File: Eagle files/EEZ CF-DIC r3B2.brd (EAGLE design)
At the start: 155 x 85 mm, 240 parts, among them IC1 MC79L05, IC2 LP2951, IC3 VIPer35L, IC4 SI8233BB-D-IS1, IC5 LM5041B, IC6 IR11688STRPBF, IC7 TL072, IC8 TL103W, IC9 TL431, P1 T910W-50K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

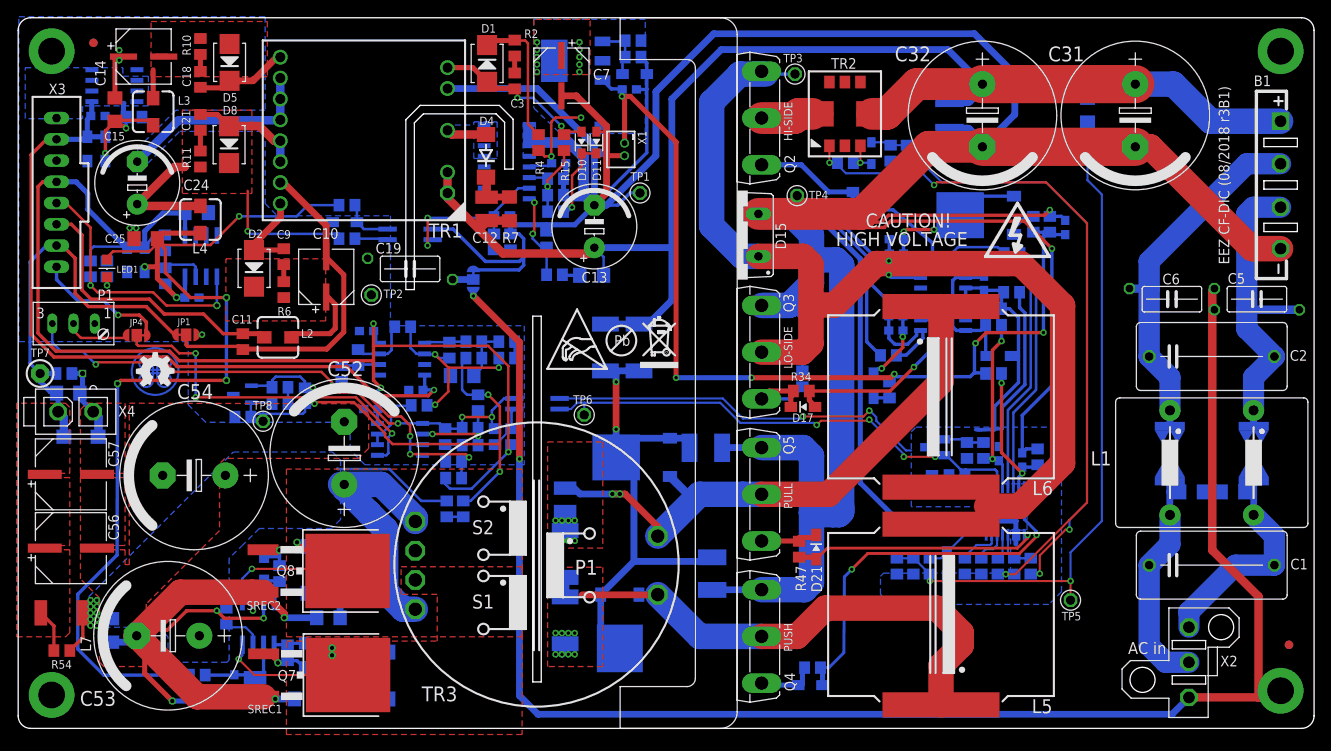
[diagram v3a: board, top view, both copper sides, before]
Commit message: BOM update, optional RC added at the output terminals
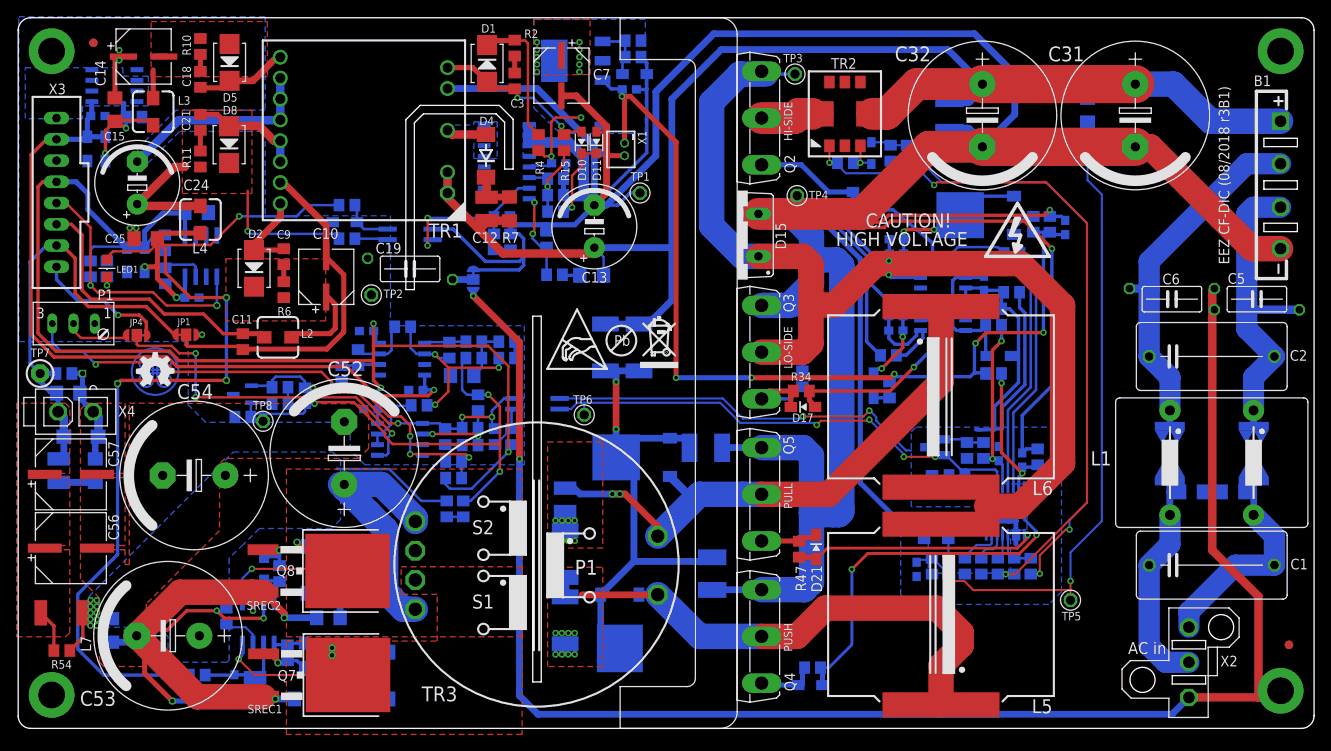
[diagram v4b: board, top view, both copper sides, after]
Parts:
- added C74: N.C., rcl:C0805
- added R80: N.C., rcl:R0805
- C42: device rcl:C0805 -> rcl:C0603
- C60: value 4n7/200V -> N.C.
- C61, C65: value 100n -> 4n7/200V; device rcl:C0603 -> rcl:C1206
- C62: value 10u -> 100n; device rcl:C1210 -> rcl:C0603
- C63: value 100n -> 10u; device rcl:C0603 -> rcl:C1210
- C64: value 4n7/200V -> 100n; device rcl:C1206 -> rcl:C0603
- C67: value 100p -> 100n; device rcl:C0805 -> rcl:C0603
- C69: value 33n -> 100p
- C70: value 4u7 -> 33n; device EEZ_Lib1:EC1206 -> rcl:C0805
- C71: value 1u -> 4u7; device rcl:C0805 -> EEZ_Lib1:EC1206
- C72: value N.C. -> 1u
- R55: value 22R/3W -> N.C.; device rcl:R2512 -> rcl:R1210
- R57: value 3R3 -> 22R/3W; device rcl:R0805 -> rcl:R2512
- R58: value 10R -> 3R3
- R59: value 47K -> 10R
- R60: value 3R3 -> 47K
- R61: value 22R/3W -> 3R3; device rcl:R2512 -> rcl:R0805
- R63: value 10K -> 22R/3W; device rcl:R0805 -> rcl:R2512
- R64: value 316K -> 10K
- R65: value 10K -> 316K
- R66: value 750R -> 10K
- R67: value 0R -> 750R
- R68: value 750R -> 0R
- R69: value 470R -> 750R
- R70: value 12K -> 470R
- R71: value 3K3 -> 12K
- R72: value 750R -> 3K3
- R73: value 30K -> 750R
- R74: value 10K -> 30K
- R75: value 16K -> 10K
- R76: value 220R -> 16K
- R77: value N.C. -> 220R
- moved C63 44.9 mm to (33.3, 6.67), turned to 270 degrees
- moved R55 42.5 mm to (9.84, 32.8), turned to 90 degrees
- moved C60 37.2 mm to (14.2, 32.8), turned to 270 degrees
- moved C64 34.6 mm to (46.7, 49.5)
- moved C65 29.2 mm to (42.1, 15.2)
- moved R78 26.0 mm to (62.0, 36.9), turned to 90 degrees
- moved R63 25.4 mm to (44.3, 21.0)
- moved R64 21.0 mm to (45.7, 46.4), turned to 270 degrees
- moved R65 20.5 mm to (56.3, 28.3), turned to 90 degrees
- moved R66 20.1 mm to (43.7, 44.5), turned to 270 degrees
- moved C72 19.4 mm to (57.1, 33.9), turned to 0 degrees
- moved R69 18.5 mm to (51.0, 50.0), turned to 0 degrees
- moved R68 13.0 mm to (63.4, 46.3)
- moved C67 11.7 mm to (47.2, 40.2), turned to 0 degrees
- moved R77 11.6 mm to (59.5, 48.3), turned to 0 degrees
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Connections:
- new net N$8: C60.2, R55.1
- net +6V: now also R59.1; no longer R58.1
- net FB: now also C73.2, R71.1, R76.2, R80.2; no longer C72.2, R70.1, R74.2, R78.2
- net GND: now also C60.1, C67.2, C71.-, C72.2, R60.2, R80.1; no longer C60.2, C70.-, C71.2, R59.2, R79.1
- net N$1: now also C68.2, R68.2, R69.1, R73.1; no longer C67.2, R67.2, R68.1, R72.1
- net N$10: now also C69.2, R75.1; no longer C68.2, R73.1
- net N$12: now also R65.1, R71.2; no longer R64.1, R70.2
- net N$132: now also R64.2, R66.1; no longer R63.2, R65.1
- net N$134: now also C68.1, R77.2; no longer C67.1, R76.2
- net N$17: now also C74.2, R79.1; no longer C73.2, R78.1
- net N$18: now also R60.1; no longer R59.1
- net N$53: now also R64.1, R69.2; no longer R63.1, R68.2
- net N$6: now also C63.1, R59.2; no longer C61.1, R58.2
- net N$64: now also R67.2, R68.1; no longer R66.2, R67.1
- net N$66: now also C61.1, R57.2; no longer C60.1, R55.2
- net N$67: now also C65.1, R63.2; no longer C64.1, R61.2
- net N$7: now also C72.1, R66.2, R72.1; no longer C71.1, R65.2, R71.1
- net N$74: now also R58.2; no longer R57.2
- net N$75: now also R61.2; no longer R60.2
- net N$76: now also C70.1, C74.1, R78.2; no longer C68.1, C72.1, R77.2
- net N$9: now also C70.2, R74.2; no longer C69.2, R73.2
- net NFB_OFFSET: now also C71.+, R67.1, R77.1; no longer C70.+, R66.1, R75.1
- net OK_A: now also R70.1, R78.1; no longer R69.1, R77.1
- net POUT+: now also R65.2; no longer R64.2
- net PREG_OUT+: now also R55.2
- net S1_DOT_OUT: now also R57.1; no longer R55.1
- net S2_OUT: now also R63.1; no longer R61.1
- net SR_OUT1: now also R58.1; no longer R57.1
- net SR_OUT2: now also R61.1; no longer R60.1
- net U_MON1: now also R73.2; no longer R72.2
- net V+: now also C64.1, C67.1, R70.2, R72.2; no longer C63.1, C66.1, R69.2, R71.2
- net V-: now also C66.1; no longer C65.1
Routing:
- net N$8: track 0.00 -> 4.38 mm
- net PREG_OUT+: track 55.2 -> 58.2 mm
- net GND: track 137.9 -> 140.7 mm
- net ULVO: track 77.4 -> 76.0 mm
- net N$25: track 7.91 -> 7.04 mm
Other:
- board text added: "C74"
- board text added: "R80"

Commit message: modified thermals for output bulk capacitors
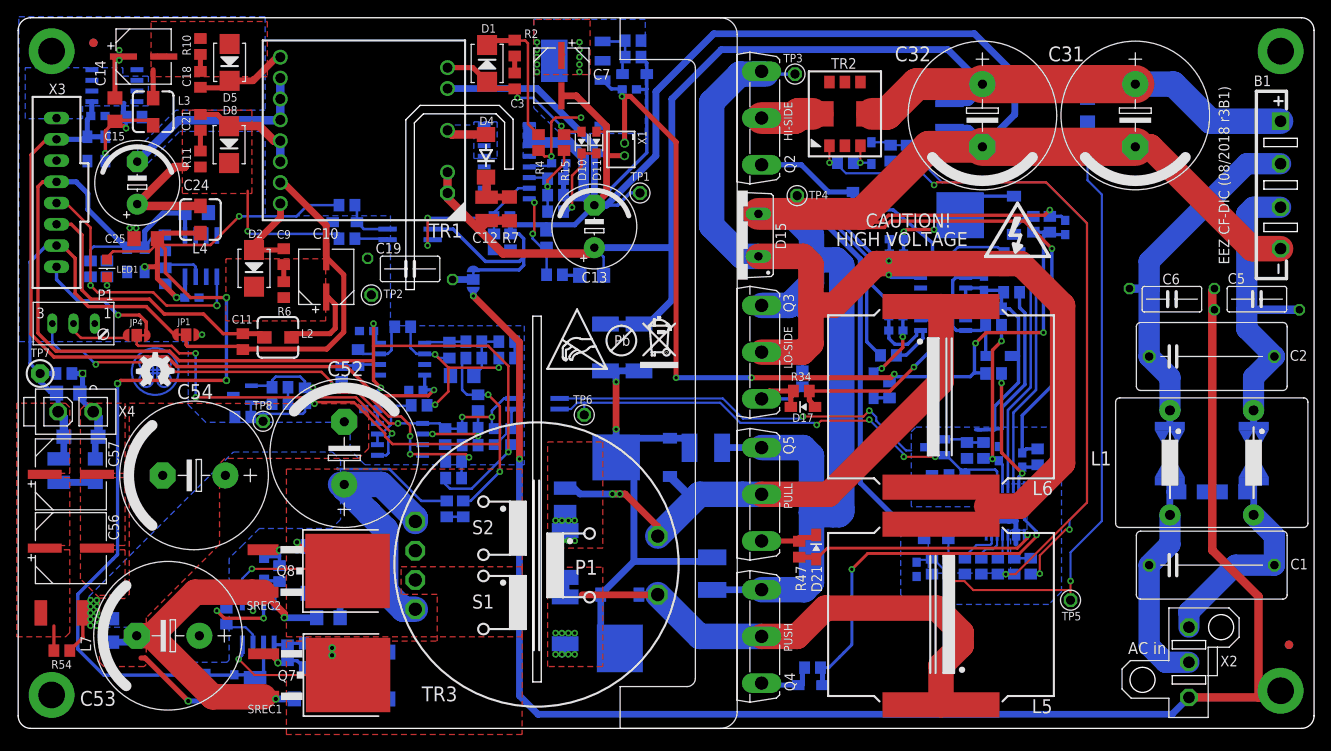
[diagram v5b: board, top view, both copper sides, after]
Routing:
- net GND: track 140.7 -> 123.9 mm
- net PREG_OUT+: track 58.2 -> 55.9 mm
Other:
- board text added: "Licensed under the TAPR Open Hardware License (www.tapr.org/OHL)"
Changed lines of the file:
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@@
 <layer number="17" name="Pads" color="14" fill="1" visible="yes" active="yes"/>
 <layer number="18" name="Vias" color="6" fill="1" visible="yes" active="yes"/>
-<layer number="19" name="Unrouted" color="6" fill="1" visible="no" active="yes"/>
+<layer number="19" name="Unrouted" color="6" fill="1" visible="yes" active="yes"/>
 <layer number="20" name="Dimension" color="4" fill="1" visible="yes" active="yes"/>
 <layer number="21" name="tPlace" color="7" fill="1" visible="yes" active="yes"/>
 <layer number="22" name="bPlace" color="6" fill="1" visible="yes" active="yes"/>
-<layer number="23" name="tOrigins" color="15" fill="1" visible="no" active="yes"/>
-<layer number="24" name="bOrigins" color="15" fill="1" visible="no" active="yes"/>
+<layer number="23" name="tOrigins" color="15" fill="1" visible="yes" active="yes"/>
+<layer number="24" name="bOrigins" color="15" fill="1" visible="yes" active="yes"/>
 <layer number="25" name="tNames" color="7" fill="1" visible="yes" active="yes"/>
 <layer number="26" name="bNames" color="5" fill="1" visible="yes" active="yes"/>
@@
 <layer number="45" name="Holes" color="7" fill="1" visible="no" active="yes"/>
 <layer number="46" name="Milling" color="3" fill="1" visible="no" active="yes"/>
-<layer number="47" name="Measures" color="7" fill="1" visible="no" active="yes"/>
+<layer number="47" name="Measures" color="7" fill="1" visible="yes" active="yes"/>
 <layer number="48" name="Document" color="7" fill="1" visible="no" active="yes"/>
 <layer number="49" name="Reference" color="7" fill="1" visible="no" active="yes"/>
@@
 <text x="112.478996875" y="24.177496875" size="1.016" layer="126" ratio="10" rot="MR0">ZD5</text>
 <text x="15.7115" y="37.512496875" size="1.27" layer="126" ratio="10" rot="MR180">ZD6</text>
+<text x="5.207" y="-1.016" size="1.27" layer="47" ratio="10">Licensed under the TAPR Open Hardware License (www.tapr.org/OHL)</text>
 </plain>
 <attributes>
@@
 </polygon>
 <wire x1="9.2735" y1="11.303" x2="9.2735" y2="14.2469" width="0.4064" layer="1"/>
-<wire x1="9.2735" y1="14.2469" x2="7.7089" y2="15.8115" width="0.4064" layer="1"/>
 <contactref element="X3" pad="2"/>
 <wire x1="23.9395" y1="49.0855" x2="23.6855" y2="49.0855" width="0.4064" layer="1"/>
@@
 <wire x1="34.3535" y1="17.205" x2="34.3535" y2="15.1765" width="0.4064" layer="16"/>
 <via x="34.3535" y="15.1765" extent="1-16" drill="0.4" shape="octagon"/>
-<via x="23.4315" y="5.2705" extent="1-16" drill="0.5" shape="octagon"/>
+<via x="25.3365" y="5.2705" extent="1-16" drill="0.5" shape="octagon"/>
 <via x="28.7655" y="16.0655" extent="1-16" drill="0.4" shape="octagon"/>
 <wire x1="28.7655" y1="16.0655" x2="29.5935" y2="16.0655" width="0.254" layer="16"/>
 <wire x1="29.5935" y1="16.0655" x2="29.9085" y2="16.3805" width="0.254" layer="16"/>
-<wire x1="23.4315" y1="5.2705" x2="23.6885" y2="5.2675" width="0.6096" layer="16"/>
-<wire x1="23.6885" y1="5.2675" x2="30.861" y2="5.2675" width="0.6096" layer="16"/>
+<wire x1="25.3365" y1="5.2705" x2="27.816" y2="5.2675" width="0.6096" layer="16"/>
+<wire x1="27.816" y1="5.2675" x2="30.861" y2="5.2675" width="0.6096" layer="16"/>
 <wire x1="30.861" y1="5.2675" x2="33.3375" y2="5.2675" width="0.6096" layer="16"/>
 <wire x1="30.861" y1="6.7065" x2="30.861" y2="5.2675" width="0.6096" layer="16"/>
-<wire x1="23.4315" y1="5.2705" x2="20.1295" y2="8.5725" width="0.6096" layer="1"/>
-<wire x1="20.1295" y1="8.5725" x2="20.1295" y2="12.446" width="0.6096" layer="1"/>
+<wire x1="25.3365" y1="5.2705" x2="20.193" y2="10.414" width="0.6096" layer="1"/>
 <contactref element="C55" pad="2"/>
 <contactref element="C61" pad="2"/>
@@
 <contactref element="C56" pad="2"/>
 <contactref element="X4" pad="2"/>
-<wire x1="34.3535" y1="5.7785" x2="26.4125" y2="5.7785" width="3.048" layer="1"/>
-<wire x1="26.4125" y1="5.7785" x2="19.1735" y2="13.081" width="3.048" layer="1"/>
+<wire x1="34.3535" y1="5.7785" x2="28.2575" y2="5.7785" width="3.048" layer="1"/>
 <wire x1="34.294" y1="18.288" x2="32.9565" y2="18.288" width="3.048" layer="1"/>
-<wire x1="32.9565" y1="18.288" x2="24.3805" y2="18.288" width="3.048" layer="1"/>
-<wire x1="24.3805" y1="18.288" x2="19.1135" y2="13.0175" width="3.048" layer="1"/>
-<wire x1="19.1135" y1="13.0175" x2="19.8755" y2="13.081" width="3.048" layer="1" curve="90"/>
-<wire x1="19.8755" y1="13.081" x2="19.1735" y2="13.081" width="3.048" layer="1"/>
+<wire x1="32.9565" y1="18.288" x2="26.162" y2="18.288" width="3.048" layer="1"/>
 <wire x1="40.7005" y1="15.24" x2="36.83" y2="15.24" width="0.8128" layer="16"/>
 <via x="36.83" y="15.24" extent="1-16" drill="0.5" shape="octagon"/>
-<wire x1="38.0335" y1="5.5245" x2="35.7505" y2="5.5245" width="0.8128" layer="16"/>
-<via x="35.7505" y="5.5245" extent="1-16" drill="0.5" shape="octagon"/>
+<wire x1="38.0335" y1="5.5245" x2="35.814" y2="5.5245" width="0.8128" layer="16"/>
+<via x="35.814" y="5.5245" extent="1-16" drill="0.5" shape="octagon"/>
 <wire x1="33.0835" y1="17.205" x2="33.0835" y2="16.0655" width="0.4064" layer="16"/>
 <via x="33.0835" y="16.0655" extent="1-16" drill="0.4" shape="octagon"/>
-<polygon width="0.254" layer="1" isolate="0.4064" thermals="no">
-<vertex x="13.208" y="40.894"/>
-<vertex x="17.78" y="40.894"/>
-<vertex x="17.78" y="32.512"/>
-<vertex x="16.002" y="32.512"/>
-<vertex x="16.002" y="32.004"/>
-<vertex x="17.78" y="32.004"/>
-<vertex x="17.78" y="23.876"/>
-<vertex x="16.002" y="23.876"/>
-<vertex x="16.002" y="23.368"/>
-<vertex x="17.78" y="23.368"/>
-<vertex x="17.78" y="21.59"/>
-<vertex x="18.288" y="21.59"/>
+<polygon width="0.254" layer="1" isolate="0.4064">
+<vertex x="18.288" y="17.9705"/>
 <vertex x="18.288" y="40.894"/>
 <vertex x="45.6565" y="40.8305"/>
@@
 <vertex x="29.718" y="34.29"/>
 <vertex x="29.083" y="33.655"/>
-<vertex x="29.083" y="25.654"/>
-<vertex x="20.32" y="16.891"/>
+<vertex x="29.083" y="24.003"/>
+<vertex x="20.32" y="15.24"/>
 <vertex x="20.32" y="9.652"/>
 <vertex x="20.066" y="9.398"/>
 <vertex x="15.24" y="9.398"/>
 <vertex x="14.732" y="9.906"/>
-<vertex x="14.732" y="17.5895"/>
-<vertex x="12.446" y="19.8755"/>
-<vertex x="12.446" y="40.132"/>
+<vertex x="14.732" y="17.907"/>
 </polygon>
 <wire x1="24.1935" y1="74.7395" x2="36.3115" y2="74.7395" width="1.016" layer="16"/>
@@
 <wire x1="36.83" y1="15.24" x2="36.83" y2="15.752" width="0.8128" layer="1"/>
 <wire x1="36.83" y1="15.752" x2="34.294" y2="18.288" width="0.8128" layer="1"/>
-<wire x1="28.7655" y1="16.0655" x2="25.146" y2="16.0655" width="0.4064" layer="1"/>
-<wire x1="25.146" y1="16.0655" x2="22.86" y2="13.7795" width="0.4064" layer="1"/>
-<wire x1="22.86" y1="13.7795" x2="19.812" y2="13.7795" width="0.4064" layer="1"/>
-<wire x1="19.812" y1="13.7795" x2="19.177" y2="13.1445" width="0.4064" layer="1"/>
 <wire x1="34.3575" y1="5.842" x2="34.3535" y2="5.5245" width="0.4064" layer="1"/>
-<wire x1="34.3535" y1="5.5245" x2="35.7505" y2="5.5245" width="0.4064" layer="1"/>
+<wire x1="34.3535" y1="5.5245" x2="35.814" y2="5.5245" width="0.4064" layer="1"/>
 <wire x1="16.1925" y1="12.316" x2="18.4085" y2="12.316" width="0.8128" layer="16"/>
 <wire x1="18.4085" y1="12.316" x2="19.1735" y2="13.081" width="0.8128" layer="16"/>
@@
 <wire x1="14.224" y1="34.2295" x2="14.224" y2="36.558" width="0.8128" layer="16"/>
 <wire x1="14.224" y1="36.558" x2="14.5595" y2="36.8935" width="0.8128" layer="16"/>
-<wire x1="34.3535" y1="5.7785" x2="34.3575" y2="5.842" width="0" layer="19" extent="1-1"/>
+<polygon width="0.254" layer="1" isolate="0.4064" thermals="no">
+<vertex x="13.208" y="40.894"/>
+<vertex x="17.78" y="40.894"/>
+<vertex x="17.78" y="32.512"/>
+<vertex x="16.002" y="32.512"/>
+<vertex x="16.002" y="32.004"/>
+<vertex x="17.78" y="32.004"/>
+<vertex x="17.78" y="23.876"/>
+<vertex x="16.002" y="23.876"/>
+<vertex x="16.002" y="23.368"/>
+<vertex x="17.78" y="23.368"/>
+<vertex x="17.78" y="17.526"/>
+<vertex x="14.732" y="17.5895"/>
+<vertex x="12.446" y="19.8755"/>
+<vertex x="12.446" y="40.132"/>
+</polygon>
+<wire x1="20.193" y1="10.414" x2="19.685" y2="10.414" width="0.6096" layer="1"/>
+<wire x1="28.2575" y1="5.7785" x2="20.955" y2="13.081" width="3.048" layer="1"/>
+<wire x1="26.162" y1="18.288" x2="20.955" y2="13.081" width="3.048" layer="1"/>
+<wire x1="20.955" y1="13.081" x2="19.1735" y2="13.081" width="3.048" layer="1"/>
+<wire x1="34.294" y1="18.288" x2="34.3535" y2="17.205" width="0" layer="19" extent="1-16"/>
+<wire x1="34.3575" y1="5.842" x2="34.3535" y2="5.7785" width="0" layer="19" extent="1-1"/>
 </signal>
 <signal name="REF">
@@
 <contactref element="Q4" pad="D"/>
 <contactref element="D19" pad="2"/>
-<polygon width="0.254" layer="1" isolate="0.3048" thermals="no">
+<polygon width="0.254" layer="1" isolate="0.3048">
 <vertex x="74.93" y="9.398"/>
 <vertex x="68.326" y="9.398"/>
@@
 <contactref element="R31" pad="1"/>
 <wire x1="70.4215" y1="27.937" x2="70.4215" y2="25.66" width="1.016" layer="16"/>
-<polygon width="0.254" layer="1" isolate="0.3048" thermals="no">
+<polygon width="0.254" layer="1" isolate="0.3048">
 <vertex x="74.93" y="23.5585"/>
 <vertex x="68.326" y="23.5585"/>
@@
 <contactref element="SH3" pad="P$1"/>
 <contactref element="SH2" pad="P$2"/>
-<polygon width="0.254" layer="16" isolate="0.4064" thermals="no" rank="3">
+<polygon width="0.254" layer="16" isolate="0.4064" rank="3">
 <vertex x="42.6085" y="35.052"/>
 <vertex x="43.561" y="34.0995"/>
@@
 </signal>
 </signals>
-<errors>
-</errors>
 </board>
 </drawing>
